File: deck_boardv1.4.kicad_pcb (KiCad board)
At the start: 2 copper layers, 135 x 50 mm, 70 parts, among them J1 430450800, J2 Conn_01x01_Pin, J3 Conn_01x01_Pin, Q1 FQPF27P06, Q2 FQPF27P06, Q3 2N7000, Q5 NMOS, SW1 SAFE_switch, SW3 SAFE_switch, U1 Raspberry Pi Zero 2 W, U2 LT8610AC, U3 DIGI XBee-PRO 900HP RF Module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, U4 ADP7159, U5 74LVC1G08

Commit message: adjustments have been made, PCB is also done
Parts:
- removed D7, D8: LED, LED_SMD:LED_0603_1608Metric
- removed D9: BZT52B12, Diode_SMD:D_SOD-123
- removed F1: 045101.5, Fuse:Fuse_1206_3216Metric
- removed F2: 1.0 A, Fuse:Fuse_1812_4532Metric
- removed L2: 2.2µH, Inductor_SMD:L_0805_2012Metric
- removed L3: 4.7µH, Inductor_SMD:L_Vishay_IHLP-2525
- removed Q5: NMOS, Package_TO_SOT_THT:TO-220-3_Vertical
- removed R15: 60.4kΩ, Resistor_SMD:R_0201_0603Metric
- removed R17: 412kΩ, Resistor_SMD:R_0201_0603Metric
- removed R18, R23: 100kΩ, Resistor_SMD:R_0201_0603Metric
- removed R19: 1 kΩ, Resistor_SMD:R_0201_0603Metric
- removed R20: 10 kΩ, Resistor_SMD:R_0201_0603Metric
- removed R21, R22: 10kΩ, Resistor_SMD:R_0201_0603Metric
- removed SW1, SW3: SAFE_switch, Connector_PinHeader_2.54mm:PinHeader_1x02_P2.54mm_Vertical
- removed U5: 74LVC1G08, Package_TO_SOT_SMD:SOT-23-5
- added C18: 47 µF, Capacitor_SMD:C_0603_1608Metric, F.Cu at (79.5, 83.2)
- added C19: 47 µF, Capacitor_SMD:C_0603_1608Metric, F.Cu at (79.5, 88.3)
- added J4: Conn_01x01_Pin, Connector_Wire:SolderWire-0.75sqmm_1x01_D1.25mm_OD2.3mm, F.Cu at (69.5, 82.5)
- added J5: Conn_01x01_Pin, Connector_Wire:SolderWire-0.75sqmm_1x01_D1.25mm_OD2.3mm, F.Cu at (75.8, 82.5)
- added J6: Conn_01x01_Pin, Connector_Wire:SolderWire-0.75sqmm_1x01_D1.25mm_OD2.3mm, F.Cu at (69.5, 89.0)
- added J7: Conn_01x01_Pin, Connector_Wire:SolderWire-0.75sqmm_1x01_D1.25mm_OD2.3mm, F.Cu at (75.8, 89.0)
- added R12: 100kΩ, Resistor_SMD:R_0201_0603Metric, F.Cu at (111.6, 64.7)
- added R13: 1.8kΩ, Resistor_SMD:R_0201_0603Metric, F.Cu at (167.4, 94.6)
- added R14: 1.8kΩ, Resistor_SMD:R_0201_0603Metric, F.Cu at (161.2, 94.6)
- C1: value 22 µF -> 47µF
- C13: value 0.1 µF -> 10µF
- C14: value 47µF -> 47pF
- C15: value 47pF -> 1µF
- C16: value 1µF -> 10µF
- C7: value 47µF -> 100µF
- C8: value 10µF -> 100µF
- D1: value SMAJ36A -> STPS5H100B; footprint Diode_SMD:D_SMA -> Schottky:DPAK
- D2: value BZT52B12 -> Red LED; footprint Diode_SMD:D_SOD-123 -> LED_SMD:LED_0603_1608Metric
- D3: value BZT52B12 -> STPS5H100B; footprint Diode_SMD:D_SOD-123 -> Schottky:DPAK
- D4: value LED -> Amber LED
- D5: value 3.6 V Zener -> Green LED; footprint Diode_SMD:D_SMA -> LED_SMD:LED_0603_1608Metric
- L1: value 2.2µH -> 10µH; footprint Inductor_SMD:L_0805_2012Metric -> Inductor_SMD:L_Vishay_IHLP-2525
- Q1: value FQPF27P06 -> MMBT3904; footprint Package_TO_SOT_SMD:SOT-223-3_TabPin2 -> Package_TO_SOT_SMD:SOT-23
- Q2: value FQPF27P06 -> 2N7002; footprint Package_TO_SOT_SMD:SOT-223-3_TabPin2 -> Package_TO_SOT_SMD:SOT-23
- Q3: value 2N7000 -> NMOS
- R1: value 100Ω -> 100kΩ
- R10: value 47Ω -> 10kΩ
- R11: value 100kΩ -> 10kΩ
- R2: value 100kΩ -> 110kΩ
- R3: value 100Ω -> 187kΩ
- R4: value 100kΩ -> 1MΩ
- R5: value 10kΩ -> 50Ω
- R6: value 100kΩ -> 45Ω
- R7: value 10kΩ -> 4.7kΩ
- U4: value ADP7159 -> ADP7158ARDZ-3.3-R7
- moved D5 112.1 mm to (179.2, 96.9)
- moved R6 107.2 mm to (179.9, 94.7), turned to 90 degrees
- moved R7 106.8 mm to (172.5, 84.8), turned to -90 degrees
- moved D2 105.8 mm to (166.7, 96.9), turned to 0 degrees
- moved R5 102.2 mm to (173.7, 94.6), turned to 90 degrees
- moved Q1 101.8 mm to (175.6, 86.2)
- moved D4 98.8 mm to (172.9, 96.9)
- moved Q2 78.7 mm to (171.7, 53.4)
- moved C14 68.6 mm to (180.6, 55.2), turned to 90 degrees
- moved Q3 61.8 mm to (139.2, 59.6)
- moved C8 39.8 mm to (89.0, 53.6), turned to -90 degrees
- moved J2 39.7 mm to (135.5, 53.5)
- moved R10 37.5 mm to (108.9, 64.7), turned to 0 degrees
- moved R9 33.5 mm to (106.8, 64.7), turned to 0 degrees
- moved R11 32.2 mm to (113.9, 64.7)
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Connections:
- C1 pad 1: Net-(C1-Pad1) -> GND
- C1 pad 2: GND -> 28V_POST-INHIB
- C13 pad 1: Net-(U5-GND) -> GND
- C13 pad 2: GND -> 3V3
- C14 pad 1: GND -> 3V3
- C14 pad 2: 5V_Pi -> GND
- C2 pad 2: /28v_inhibit/28V_Post_Inhibit -> 28V_POST-INHIB
- C8 pad 2: 3V3 -> 5V_Pi
- C9 pad 1: GND -> Net-(U4-REF)
- C9 pad 2: Net-(U4-REF) -> GND
- D1 pad 1: Net-(D1-A1) -> (no net)
- D1 pad 2: GND -> Net-(J4-Pin_1)
- D2 pad 1: Net-(D1-A1) -> GND
- D3 pad 1: /28v_inhibit/POST_INHIB1 -> (no net)
- D3 pad 2: Net-(D3-A) -> Net-(J6-Pin_1)
- D5 pad 1: /Burn-Wire Circuit/ENABLE -> Net-(D5-K)
- D5 pad 2: GND -> Net-(D5-A)
- J1 pad 1: /28v_inhibit/28v_IN -> 28V
- J2 pad 1: Net-(J2-Pin_1) -> ENABLE
- L1 pad 1: Net-(Q1-S) -> Net-(C6-Pad1)
- L1 pad 2: Net-(C1-Pad1) -> 5V_Pi
- Q1 pad 1: Net-(Q1-G) -> Net-(Q1-B)
- Q1 pad 2: Net-(Q1-S) -> GND
- Q1 pad 3: Net-(D1-A1) -> Net-(D5-K)
- Q2 pad 1: Net-(Q2-G) -> GPIO24
- Q2 pad 2: /28v_inhibit/28V_Post_Inhibit -> GND
- Q2 pad 3: /28v_inhibit/POST_INHIB1 -> XBee_RESET
- Q3 pad 1: Net-(D3-A) -> Net-(J3-Pin_1)
- Q3 pad 2: Net-(Q3-G) -> ENABLE
- R1 pad 1: Net-(Q1-G) -> Net-(U2-PG)
- R1 pad 2: Net-(D2-A) -> 5V_Pi
- R10 pad 1: Net-(Q5-G) -> Net-(U1-GPIO17-Camera_Select/TE-1)
- R10 pad 2: Net-(R10-Pad2) -> GND
- R11 pad 1: GND -> Net-(U1-GPIO22-TE-2)
- R11 pad 2: Net-(Q5-G) -> GND
- R16 pad 2: Net-(U2-FB) -> ENABLE
- R2 pad 1: Net-(D2-A) -> Net-(U2-RT)
- R3 pad 1: Net-(Q2-G) -> GND
- R3 pad 2: Net-(D3-A) -> Net-(U2-FB)
- R4 pad 1: Net-(D3-A) -> Net-(U2-FB)
- R4 pad 2: /28v_inhibit/POST_INHIB1 -> 5V_Pi
- R5 pad 1: Net-(Q3-G) -> Net-(D4-A)
- R5 pad 2: Net-(D9-K) -> 3V3
- R6 pad 1: GND -> Net-(D5-A)
- R6 pad 2: Net-(D9-K) -> 3V3
- R7 pad 1: /Burn-Wire Circuit/ENABLE -> XBee_ASSOC
- R7 pad 2: TE_2 -> Net-(Q1-B)
- R8 pad 1: /Burn-Wire Circuit/ENABLE -> GPIO24
- R8 pad 2: GND -> 3V3
- R9 pad 1: /Burn-Wire Circuit/CTRL_IN -> TE_1
- R9 pad 2: GND -> Net-(U1-GPIO17-Camera_Select/TE-1)
- U1 pad 11: TE_1 -> Net-(U1-GPIO17-Camera_Select/TE-1)
- U1 pad 13: /Burn-Wire Circuit/CTRL_IN -> unconnected-(U1-GPIO27-Pad13)
- U1 pad 15: TE_2 -> Net-(U1-GPIO22-TE-2)
- U1 pad 16: unconnected-(U1-GPIO23/GPIO_GEN4-Pad16) -> XBee_ASSOC
- U1 pad 18: unconnected-(U1-GPIO24/GPIO_GEN5-Pad18) -> GPIO24
- U2 pad 1: unconnected-(U2-SYNC-Pad1) -> GND
- U2 pad 4: /28v_inhibit/28V_Post_Inhibit -> 28V_POST-INHIB
- U2 pad 5: /28v_inhibit/28V_Post_Inhibit -> 28V_POST-INHIB
- U2 pad 6: /28v_inhibit/28V_Post_Inhibit -> 28V_POST-INHIB
- U3 pad 15: Net-(U3-ASSOCIATE/AD5/DIO5) -> XBee_ASSOC
- U3 pad 5: unconnected-(U3-~{RESET}-Pad5) -> XBee_RESET
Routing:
- net ENABLE: track 0.00 -> 174.6 mm, vias 0 -> 4
- net 28V_POST-INHIB: track 0.00 -> 152.9 mm, vias 0 -> 2
- net /Burn-Wire Circuit/ENABLE: track 101.2 -> 0.00 mm, vias 2 -> 0
- net XBee_ASSOC: track 0.00 -> 79.2 mm, vias 0 -> 1
- net /Burn-Wire Circuit/CTRL_IN: track 77.7 -> 0.00 mm, vias 2 -> 0
- net GPIO24: track 0.00 -> 63.1 mm
- net Net-(D7-K): track 49.0 -> 0.00 mm
- net /28v_inhibit/POST_INHIB1: track 46.9 -> 0.00 mm
- net 3V3: track 103.1 -> 140.8 mm, vias 0 -> 2
- net Net-(J3-Pin_1): track 41.8 -> 6.08 mm
- net Net-(D9-K): track 26.8 -> 0.00 mm
- net /28v_inhibit/28V_Post_Inhibit: track 25.5 -> 0.00 mm
- net GND: track 27.7 -> 6.30 mm, vias 1 -> 3
- net Net-(J4-Pin_1): track 0.00 -> 14.5 mm
- net Net-(U3-ASSOCIATE/AD5/DIO5): track 12.8 -> 0.00 mm
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
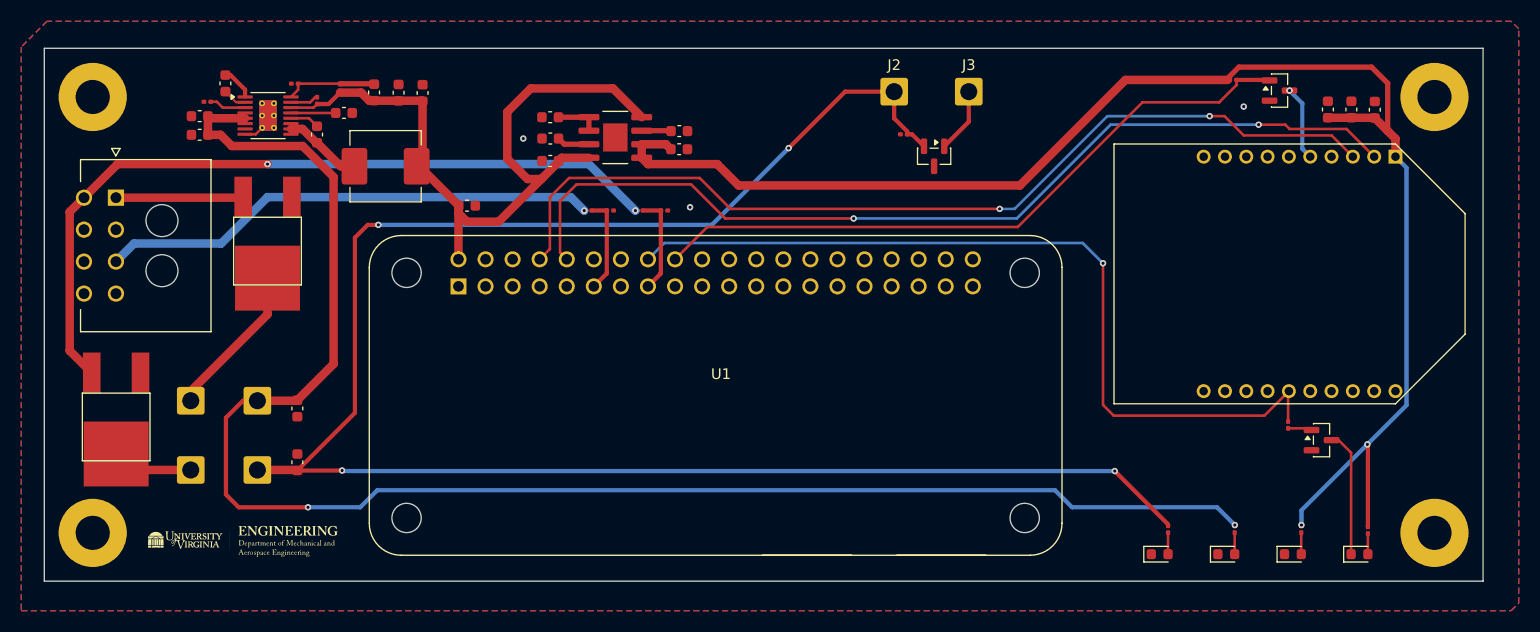
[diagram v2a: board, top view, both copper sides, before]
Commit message: Resolved errors and warnings.
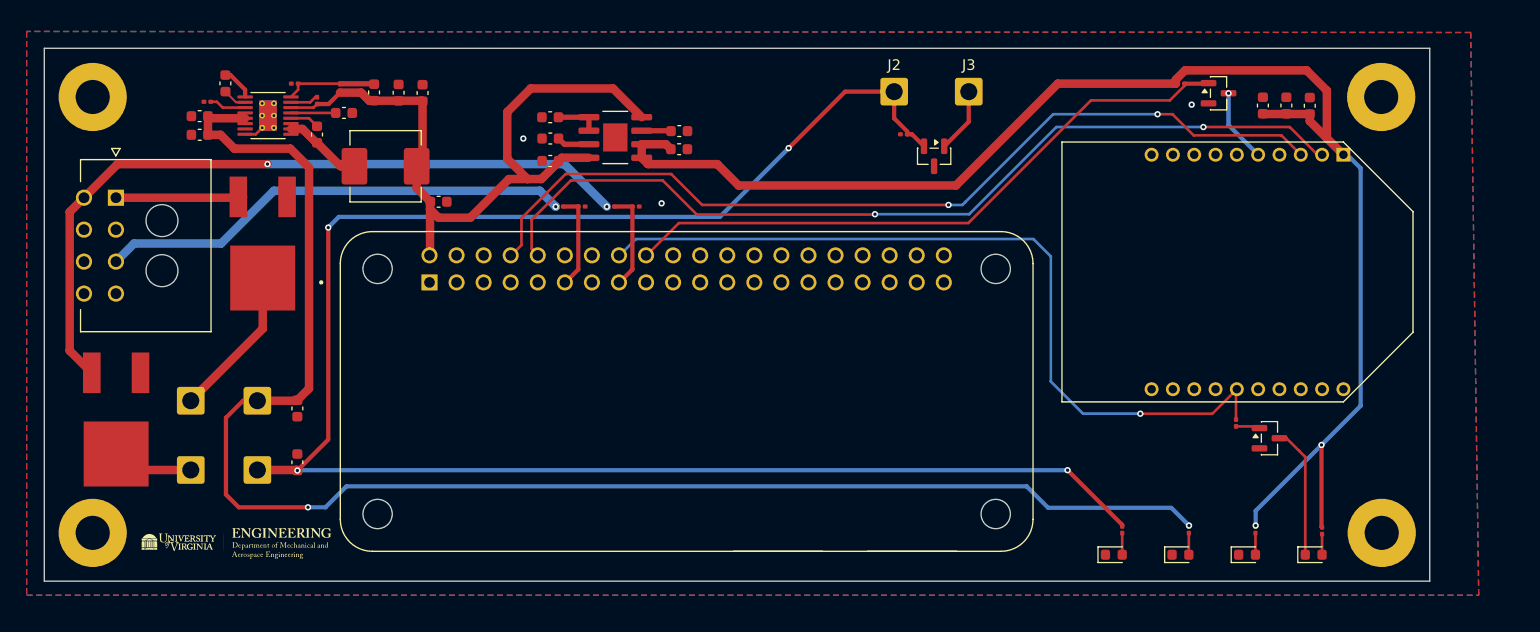
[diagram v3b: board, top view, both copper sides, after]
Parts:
- U1: footprint Raspberry Pi Zero 2 W:MODULE_SC1176 -> SC1176:MODULE_SC1176
- moved C14 6.11 mm to (174.5, 54.8)
- moved C15 6.11 mm to (172.3, 54.8)
- moved C16 6.11 mm to (170.1, 54.8)
- moved Q2 5.73 mm to (165.9, 53.6)
- moved ? 5.00 mm to (181.2, 54.0)
- moved ? 4.95 mm to (181.2, 94.9)
- moved R8 4.90 mm to (162.4, 52.8)
- moved R7 4.89 mm to (167.6, 84.6)
- moved Q1 4.89 mm to (170.7, 86.0)
- moved U3 4.89 mm to (167.7, 70.4)
- moved D2 4.30 mm to (162.4, 97.0)
- moved D4 4.30 mm to (168.6, 97.0)
- moved D5 4.30 mm to (174.9, 97.0)
- moved D6 4.30 mm to (156.1, 97.0)
- moved R13 4.30 mm to (163.2, 94.6)
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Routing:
- net 28V_POST-INHIB: track 152.9 -> 146.2 mm
- net 3V3: track 140.8 -> 135.9 mm
- net GPIO15: track 89.0 -> 85.1 mm
- net GPIO14: track 88.7 -> 85.1 mm
- net GPIO24: track 63.1 -> 59.5 mm
- net XBee_ASSOC: track 79.2 -> 76.1 mm
- net TE_2: track 72.7 -> 69.9 mm
- net TE_1: track 47.0 -> 44.6 mm
- net ENABLE: track 174.6 -> 172.4 mm
- net Net-(J4-Pin_1): track 14.5 -> 15.2 mm
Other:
- board size 135 x 50 mm -> 130 x 50 mm

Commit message: Resolved manufacturer design rules
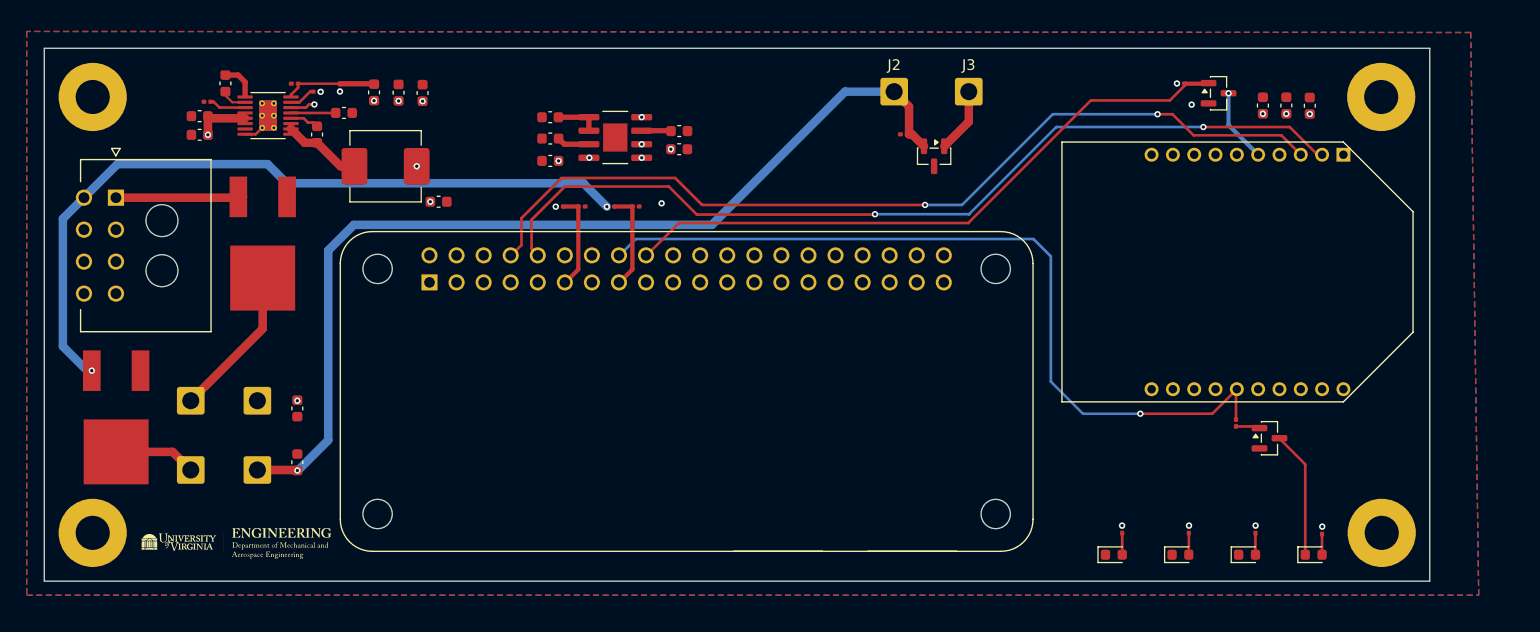
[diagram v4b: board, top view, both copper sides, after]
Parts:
- moved R1 0.84 mm to (81.3, 53.5), turned to 0 degrees
- moved D3 0.20 mm to (62.5, 84.8)
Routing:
- net 3V3: track 135.9 -> 0.82 mm, vias 2 -> 9
- net 5V_Pi: track 68.1 -> 3.59 mm, vias 0 -> 11
- net ENABLE: track 172.4 -> 171.1 mm, vias 4 -> 2
- net TE_2: track 69.9 -> 70.7 mm
- net 28V_POST-INHIB: track 146.2 -> 146.8 mm, vias 2 -> 3
- net GND: track 6.30 -> 6.68 mm, vias 3 -> 2
- added copper zone on In2.Cu, net 3V3
- added copper zone on In1.Cu, net 5V_Pi
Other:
- copper layers 2 -> 4
- rule pad_to_mask_clearance: 0 -> 0.0508
